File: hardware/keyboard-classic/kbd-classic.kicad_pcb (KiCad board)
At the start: 2 copper layers, 348 x 112.8 mm, 141 parts, among them J1 Controller, SW1 RT Arrow, SW10 Bracket_Open, SW11 6, SW12 Y, SW13 Return, SW14 Dash, SW15 5, SW16 T, SW17 Line Feed, SW18 Colon, SW19 4, SW2 LT Arrow, SW20 R, SW21 O, SW22 0, SW23 3, SW24 E, SW25 L, SW26 9, SW27 2, SW28 W, SW29 Period, SW3 Tilde, SW30 8, SW31 1, SW32 @ (OSI shift lock), SW33 Break, SW34 Rubout (OSI Break), SW35 R_Shift, SW36 P, SW37 Comma, SW38 K, SW39 L_Shift, SW4 I, SW40 Semicolon, SW41 M, SW42 J, SW43 Fwd_Slash, SW44 N, SW45 H, SW46 SPACE, SW47 B, SW48 G, SW49 TAB, SW5 Repeat, SW50 Z, SW51 V, SW52 F, SW53 CTRL, SW54 A, SW55 C, SW56 D, SW57 Backslash, SW58 Q, SW59 X, SW6 Bracket_Close, SW60 S, SW61 Power light, SW62 ESC, SW63 Spare, SW7 7, SW8 U, SW9 Caps_Lock

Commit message: Update the spacing comment to include spacing for keyboard cutout
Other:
- board text added: "Distances: Vertical: 0.75 inch Horizontal (1x - 1x): 0.75 inch Horizontal (1x - 1.5x): 0.9375 inch Horizontal (Row 1 left key -> Row 2 left key): 0.375 inch Horizontal (Row 2 left key -> Row 3 left key): 0.1875 inch Horizontal (Row 3 left key -> Row 4 left key): 0.1875 inch Horizontal (Row 4 left key -> Row 5 left key): -0.1875 inch Horizontal (Row 5 left key -> Space bar): 4.5 inch Center of key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"
- board text removed: "Distances: Vertical: 0.75 inch Horizontal (1x - 1x): 0.75 inch Horizontal (1x - 1.5x): 0.9375 inch Horizontal (Row 1 left key -> Row 2 left key): 0.375 inch Horizontal (Row 2 left key -> Row 3 left key): 0.1875 inch Horizontal (Row 3 left key -> Row 4 left key): 0.1875 inch Horizontal (Row 4 left key -> Row 5 left key): -0.1875 inch Horizontal (Row 5 left key -> Space bar): 4.5 inch"
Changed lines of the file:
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@@
   (gr_line (start 33.64738 180.34) (end 381.64738 180.34) (layer Edge.Cuts) (width 0.1))
   (gr_line (start 381.64738 67.564) (end 33.64738 67.564) (layer Edge.Cuts) (width 0.1))
-  (gr_text "Distances:\nVertical: 0.75 inch\nHorizontal (1x - 1x): 0.75 inch\nHorizontal (1x - 1.5x): 0.9375 inch\nHorizontal (Row 1 left key -> Row 2 left key): 0.375 inch\nHorizontal (Row 2 left key -> Row 3 left key): 0.1875 inch\nHorizontal (Row 3 left key -> Row 4 left key): 0.1875 inch\nHorizontal (Row 4 left key -> Row 5 left key): -0.1875 inch\nHorizontal (Row 5 left key -> Space bar): 4.5 inch" (at 38.4175 240.0681) (layer Cmts.User)
+  (gr_text "Distances:\nVertical: 0.75 inch\nHorizontal (1x - 1x): 0.75 inch\nHorizontal (1x - 1.5x): 0.9375 inch\nHorizontal (Row 1 left key -> Row 2 left key): 0.375 inch\nHorizontal (Row 2 left key -> Row 3 left key): 0.1875 inch\nHorizontal (Row 3 left key -> Row 4 left key): 0.1875 inch\nHorizontal (Row 4 left key -> Row 5 left key): -0.1875 inch\nHorizontal (Row 5 left key -> Space bar): 4.5 inch\nCenter of key to cutout edge: 0.36 inch" (at 38.4175 240.0681) (layer Cmts.User)
     (effects (font (size 2.54 2.54) (thickness 0.3048)) (justify left))
   )

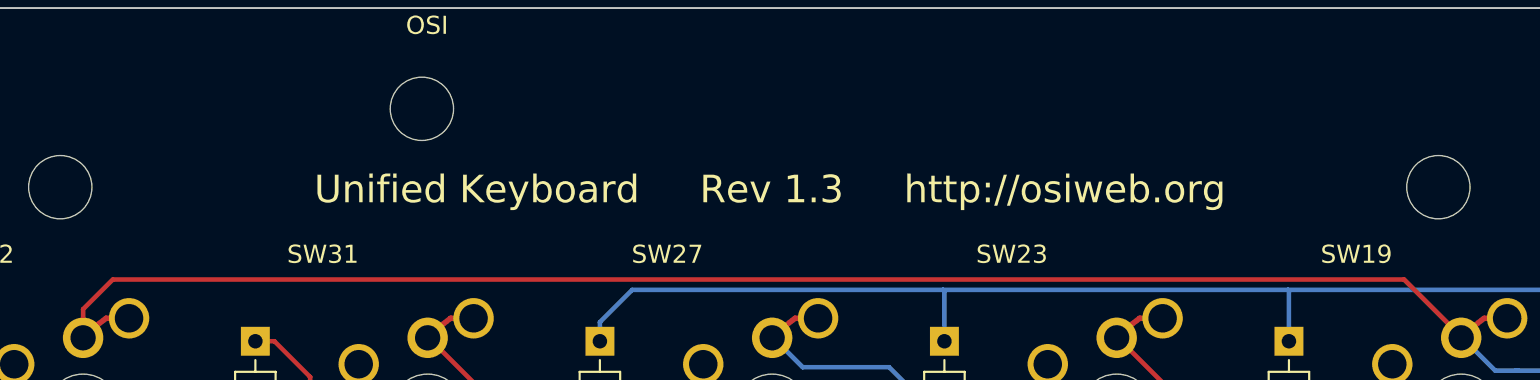
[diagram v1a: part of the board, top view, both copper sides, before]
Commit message: Update rev to 1.4
pcb: ajust cutout to account for 1.5u wide LEFT SHIFT
schematic: minor text format cleanup
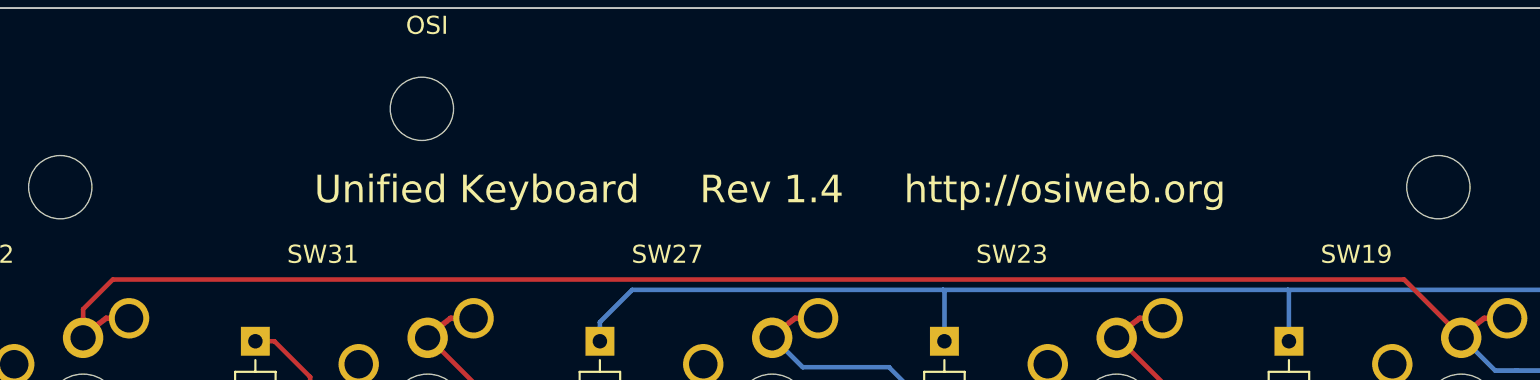
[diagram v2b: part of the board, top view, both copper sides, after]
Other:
- board text added: "Distances: Vertical: 0.75 inch Horizontal (1u - 1u): 0.75 inch Horizontal (1u - 1.5u): 0.9375 inch Horizontal (Row 1 left key -> Row 2 left key): 0.375 inch Horizontal (Row 2 left key -> Row 3 left key): 0.1875 inch Horizontal (Row 3 left key -> Row 4 left key): 0.1875 inch Horizontal (Row 4 left key -> Row 5 left key): -0.1875 inch Horizontal (Row 5 left key -> Space bar): 4.5 inch Center of key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"
- board text added: "Unified Keyboard Rev 1.4 http://osiweb.org"
- board text removed: "Distances: Vertical: 0.75 inch Horizontal (1x - 1x): 0.75 inch Horizontal (1x - 1.5x): 0.9375 inch Horizontal (Row 1 left key -> Row 2 left key): 0.375 inch Horizontal (Row 2 left key -> Row 3 left key): 0.1875 inch Horizontal (Row 3 left key -> Row 4 left key): 0.1875 inch Horizontal (Row 4 left key -> Row 5 left key): -0.1875 inch Horizontal (Row 5 left key -> Space bar): 4.5 inch Center of key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"
- board text removed: "Unified Keyboard Rev 1.3 http://osiweb.org"
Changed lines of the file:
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@@
   (general
     (thickness 1.6)
-    (drawings 44)
+    (drawings 40)
     (tracks 1105)
     (zones 0)
@@
     (title "Unified Retro Keyboard")
     (date 2019-08-25)
-    (rev 1.3)
+    (rev 1.4)
     (company OSIWeb.org)
     (comment 1 "Key matrix w/ LED")
@@
     (visible_elements 7FFFEFFF)
     (pcbplotparams
-      (layerselection 0x01000_7ffffffe)
+      (layerselection 0x11000_7ffffffe)
       (usegerberextensions false)
       (usegerberattributes false)
@@
   (gr_arc (start 376.64738 89.79916) (end 376.64738 91.57716) (angle -180) (layer Edge.Cuts) (width 0.1016))
   (gr_arc (start 376.64738 165.99916) (end 376.64738 167.77716) (angle -180) (layer Edge.Cuts) (width 0.1016))
-  (gr_line (start 73.71588 137.04316) (end 73.71588 117.99316) (layer B.Fab) (width 0.15))
-  (gr_line (start 73.71588 156.85516) (end 73.71588 175.14316) (layer B.Fab) (width 0.15))
-  (gr_line (start 78.47838 156.85516) (end 73.71588 156.85516) (layer B.Fab) (width 0.15))
-  (gr_line (start 78.47838 137.04316) (end 73.71588 137.04316) (layer B.Fab) (width 0.15))
-  (gr_line (start 78.47838 137.04316) (end 78.47838 156.85516) (layer B.Fab) (width 0.15))
+  (gr_line (start 73.71588 175.14316) (end 73.71588 117.99316) (layer B.Fab) (width 0.15))
   (gr_line (start 59.42838 98.94316) (end 68.95338 98.94316) (layer B.Fab) (width 0.15))
   (gr_line (start 43.17238 88.02116) (end 33.64738 88.02116) (layer Edge.Cuts) (width 0.1016))
@@
   (gr_line (start 33.64738 167.77716) (end 33.64738 180.34) (layer Edge.Cuts) (width 0.1016))
   (gr_arc (start 43.17238 89.79916) (end 43.17238 91.57716) (angle -180) (layer Edge.Cuts) (width 0.1016))
-  (gr_text "Unified Keyboard     Rev 1.3     http://osiweb.org" (at 106.553 77.597) (layer F.SilkS)
+  (gr_text "Unified Keyboard     Rev 1.4     http://osiweb.org" (at 106.553 77.597) (layer F.SilkS)
     (effects (font (size 1.524 1.524) (thickness 0.1778)))
   )
@@
   (gr_line (start 33.64738 180.34) (end 381.64738 180.34) (layer Edge.Cuts) (width 0.1))
   (gr_line (start 381.64738 67.564) (end 33.64738 67.564) (layer Edge.Cuts) (width 0.1))
-  (gr_text "Distances:\nVertical: 0.75 inch\nHorizontal (1x - 1x): 0.75 inch\nHorizontal (1x - 1.5x): 0.9375 inch\nHorizontal (Row 1 left key -> Row 2 left key): 0.375 inch\nHorizontal (Row 2 left key -> Row 3 left key): 0.1875 inch\nHorizontal (Row 3 left key -> Row 4 left key): 0.1875 inch\nHorizontal (Row 4 left key -> Row 5 left key): -0.1875 inch\nHorizontal (Row 5 left key -> Space bar): 4.5 inch\nCenter of key to cutout edge: 0.36 inch" (at 38.4175 240.0681) (layer Cmts.User)
+  (gr_text "Distances:\nVertical: 0.75 inch\nHorizontal (1u - 1u): 0.75 inch\nHorizontal (1u - 1.5u): 0.9375 inch\nHorizontal (Row 1 left key -> Row 2 left key): 0.375 inch\nHorizontal (Row 2 left key -> Row 3 left key): 0.1875 inch\nHorizontal (Row 3 left key -> Row 4 left key): 0.1875 inch\nHorizontal (Row 4 left key -> Row 5 left key): -0.1875 inch\nHorizontal (Row 5 left key -> Space bar): 4.5 inch\nCenter of key (1u) to vertical or side cutout edge: 0.36 inch\nCenter of key (1.5u) to side cutout edge: 0.5475 inch" (at 38.4175 240.0681) (layer Cmts.User)
     (effects (font (size 2.54 2.54) (thickness 0.3048)) (justify left))
   )

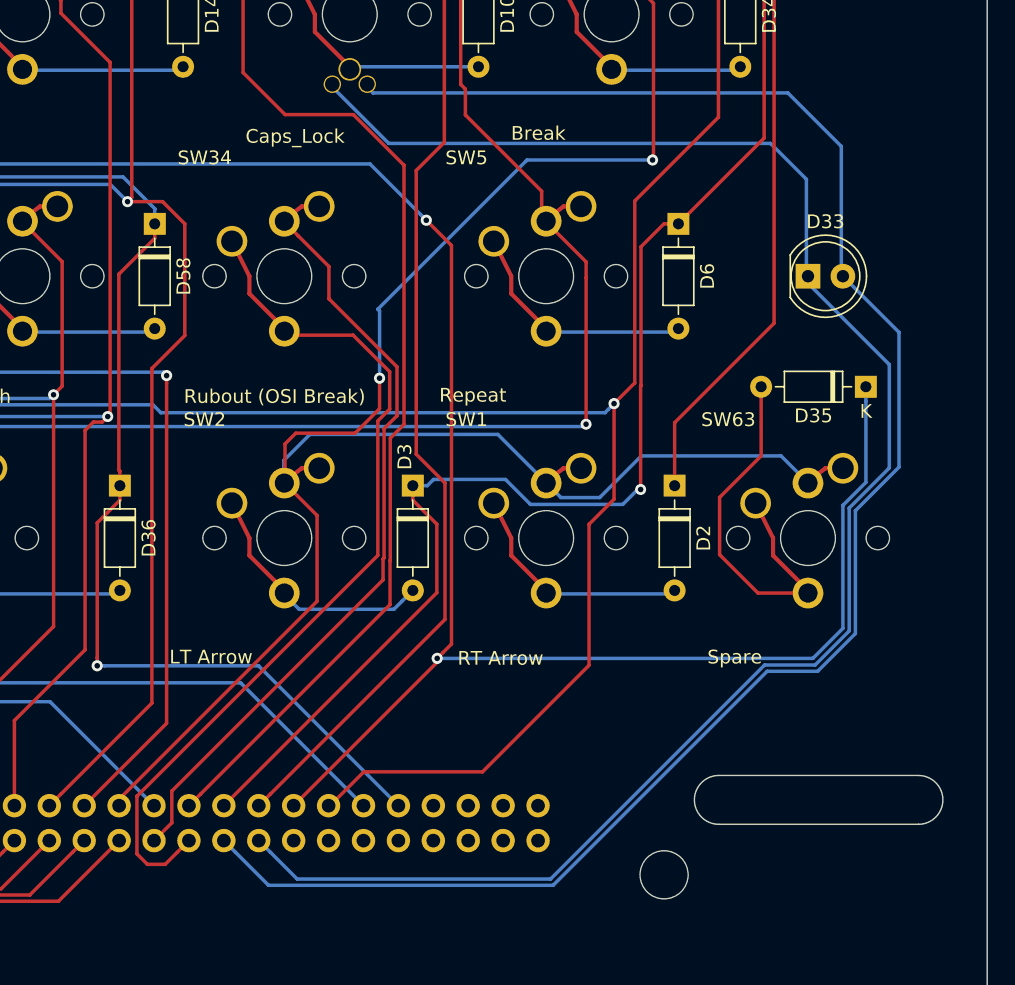
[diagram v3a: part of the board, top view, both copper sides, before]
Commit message: Moved spare LED from caps-lock to @ (OSI shift LOCK)
This allows the keymap to determine which LED is used, rather than requiring the
decision to be hardwired in at the time of assembly.  For the OSI keyboard, the
LED could be placed on the SHIFTLOCK key, at the far right LED, or in the
CAPSLOCK position, which is just to the left of the RETURN and not otherwise
populated in the OSI layout.
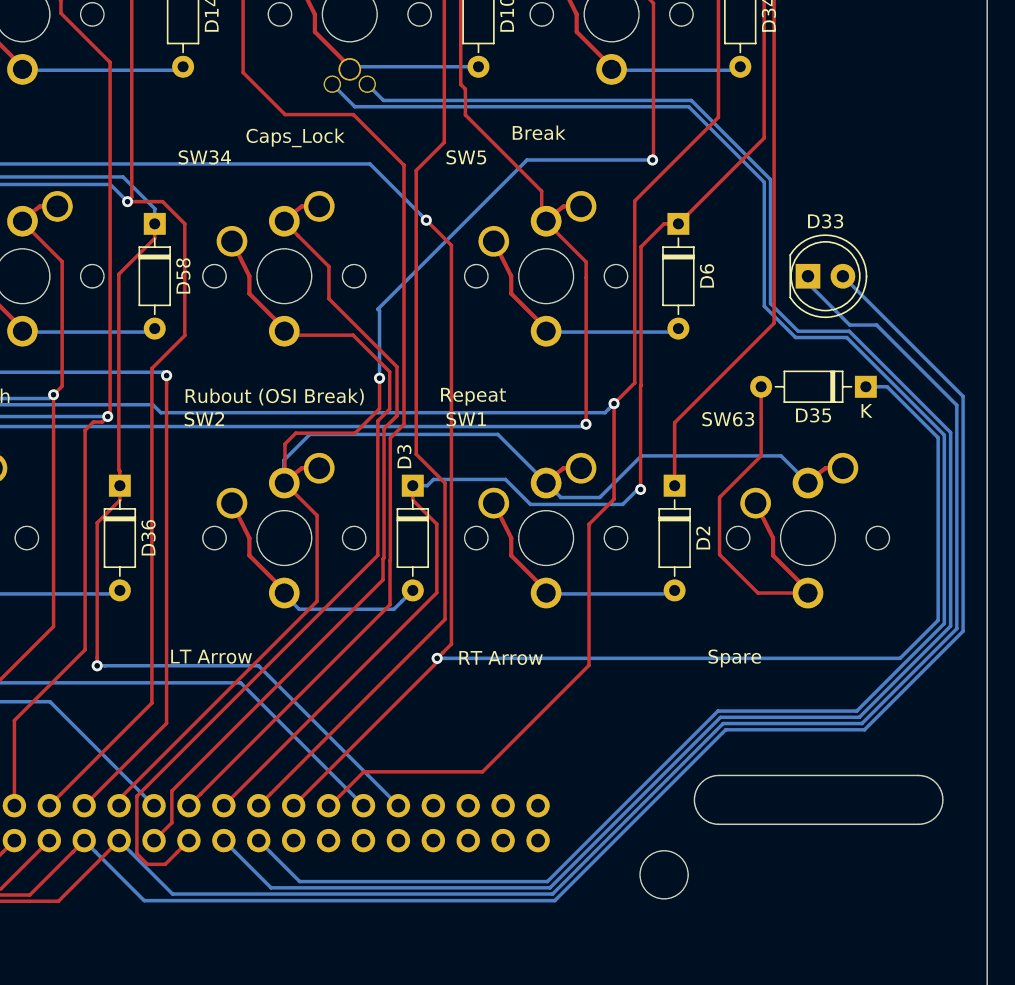
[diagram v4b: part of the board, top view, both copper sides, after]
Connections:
- J1 pad 14: Net-(J1-Pad14) -> Net-(D33-Pad2)
- J1 pad 16: Net-(J1-Pad16) -> Net-(D33-Pad1)
- J1 pad 22: Net-(D33-Pad2) -> Net-(J1-Pad22)
- J1 pad 24: Net-(D33-Pad1) -> Net-(J1-Pad24)
- SW32 pad 3: Net-(J1-Pad16) -> Net-(D33-Pad1)
- SW32 pad 4: Net-(J1-Pad14) -> Net-(D33-Pad2)
- SW9 pad 3: Net-(D33-Pad1) -> Net-(J1-Pad24)
- SW9 pad 4: Net-(D33-Pad2) -> Net-(J1-Pad22)
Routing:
- net Net-(J1-Pad22): track 0.00 -> 134.5 mm
- net Net-(J1-Pad24): track 0.00 -> 133.0 mm
- net Net-(J1-Pad16): track 68.5 -> 0.00 mm
- net Net-(J1-Pad14): track 61.5 -> 0.00 mm
- net Net-(D33-Pad1): track 125.7 -> 170.0 mm
- net Net-(D33-Pad2): track 129.9 -> 164.8 mm
- net /Row3: track 339.0 -> 348.0 mm

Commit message: Move LED current limit resistors to keyboard PCB
For better matching of current limit resistors to LEDs, the resistors are moved
to the keyboard matrix PCB, where they can be tuned for maximum brightness (at
100% duty cycle).  This allows consistent keyboard brightness when a single
interface PCB is swapped between keyboard matrices.
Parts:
- added R1: 470, Resistor_THT:R_Axial_DIN0207_L6.3mm_D2.5mm_P10.16mm_Horizontal, F.Cu at (69.8, 152.4)
- added R2: 470, Resistor_THT:R_Axial_DIN0207_L6.3mm_D2.5mm_P10.16mm_Horizontal, F.Cu at (310.4, 176.9)
- added R3: 470, Resistor_THT:R_Axial_DIN0207_L6.3mm_D2.5mm_P10.16mm_Horizontal, F.Cu at (370.8, 116.8)
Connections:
- J1 pad 14: Net-(D33-Pad2) -> Net-(J1-Pad14)
- SW61 pad 3: Net-(J1-Pad8) -> Net-(R1-Pad1)
- SW9 pad 4: Net-(J1-Pad22) -> Net-(R3-Pad2)
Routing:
- net Net-(R3-Pad2): track 0.00 -> 40.2 mm
- net Net-(J1-Pad22): track 134.5 -> 108.3 mm
- net Net-(R1-Pad1): track 0.00 -> 24.5 mm
- net Net-(J1-Pad8): track 246.6 -> 261.8 mm
- net Net-(J1-Pad14): track 0.00 -> 10.7 mm
- net Net-(D33-Pad2): track 164.8 -> 174.0 mm, vias 0 -> 1
- net Net-(J1-Pad10): track 62.3 -> 63.6 mm
- net Net-(J1-Pad12): track 60.8 -> 61.6 mm
- net Net-(D33-Pad1): track 170.0 -> 169.5 mm

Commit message: Multiple fixes to classic keyboard for fit and build ease
- remove material from PCB to allow keyboard to fit in Apple II case

- enlarge center hole on cherry MX footprints slightly, to 0.160" to allow
slightly more tolerance, which eases assembly.

- include holes for LEDs on futaba aligner

- include extra pads on main PCB for LEDs with futaba keys

- Add LED on LINE FEED which maps to REPEAT/CAPSLOCK on Apple II keymap
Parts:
- removed the REF** at (263.8, 174.3)
- removed the REF** at (263.8, 159.0)
- removed Stabilizer (x2): MountingHole_3.5mm, MountingHole:MountingHole_3.5mm
- added D62: LED, LED_THT:LED_D2.0mm_W4.8mm_H2.5mm_FlatTop, F.Cu at (84.1, 175.5)
- added D63: LED, LED_THT:LED_D2.0mm_W4.8mm_H2.5mm_FlatTop, F.Cu at (334.1, 118.4)
- added D64: LED, LED_THT:LED_D2.0mm_W4.8mm_H2.5mm_FlatTop, F.Cu at (293.7, 137.4)
- added D65: LED, LED_THT:LED_D2.0mm_W4.8mm_H2.5mm_FlatTop, F.Cu at (286.5, 118.4)
- SW17: value Line Feed -> Line_Feed; footprint unikbd:Key_MX -> unikbd:Key_MX_LED
- SW32: value @ (OSI shift lock) -> @ (OSI ShiftLock)
- SW46: footprint unikbd:Key_MX -> unikbd:Key_MX_Spacebar_5.25
- SW61: value Power light -> Power Light
- moved D33 3.81 mm to (364.8, 127.9)
- moved R3 2.79 mm to (368.0, 116.8)
- moved D4 2.54 mm to (368.0, 95.0)
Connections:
- J1 pad 24: Net-(J1-Pad24) -> Net-(D63-Pad1)
- J1 pad 8: Net-(J1-Pad8) -> Net-(D62-Pad1)
- R1 pad 2: Net-(J1-Pad8) -> Net-(J1-Pad6)
- R3 pad 2: Net-(R3-Pad2) -> Net-(D63-Pad2)
- SW17 pad 3: (no net) -> Net-(D63-Pad1)
- SW17 pad 4: (no net) -> Net-(D63-Pad2)
- SW32 pad 3: Net-(D33-Pad1) -> Net-(D33-Pad2)
- SW32 pad 4: Net-(D33-Pad2) -> Net-(D33-Pad1)
- SW61 pad 4: Net-(J1-Pad6) -> Net-(D62-Pad1)
- SW9 pad 3: Net-(J1-Pad24) -> Net-(D63-Pad1)
- SW9 pad 4: Net-(R3-Pad2) -> Net-(D63-Pad2)
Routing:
- net Net-(J1-Pad8): track 261.8 -> 0.00 mm
- net Net-(D62-Pad1): track 0.00 -> 248.0 mm, vias 0 -> 1
- net Net-(D63-Pad1): track 0.00 -> 196.7 mm
- net Net-(J1-Pad24): track 132.9 -> 0.00 mm
- net Net-(D63-Pad2): track 0.00 -> 110.9 mm
- net Net-(R3-Pad2): track 40.2 -> 0.00 mm
- net Net-(J1-Pad6): track 240.2 -> 259.7 mm
- net Net-(D33-Pad2): track 174.0 -> 188.8 mm, vias 1 -> 2
- net /Row6: track 276.0 -> 284.2 mm
- net Net-(J1-Pad22): track 108.3 -> 114.4 mm
- net Net-(D4-Pad2): track 22.5 -> 17.3 mm
- net Net-(D62-Pad2): track 24.5 -> 29.1 mm
- net /Row5: track 275.8 -> 271.8 mm, vias 2 -> 3
- net Net-(D33-Pad1): track 169.5 -> 171.8 mm
- net /Col7: track 385.5 -> 387.3 mm
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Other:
- outline, holes or cut-outs redrawn

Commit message: Fixes for classic keyboard outline and mounting hole patters
- Adjust upper right corner circular cutout for AppleII+ case fit.

- Adjust OSI mounting hole pattern for improved fit.

- Changed OSI mount holes along top of keyboard to slots, to fit both C2P (542
keyboard) and C4P (542 Rev B/c keyboards).

- PCB and aligners must be slightly taller to accommodate the slots along the
top row
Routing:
- net Net-(D63-Pad1): track 196.7 -> 195.0 mm
- net /Row3: track 349.3 -> 348.6 mm
- net Net-(D33-Pad2): track 188.8 -> 188.2 mm
- net Net-(J1-Pad22): track 114.4 -> 113.9 mm
- net Net-(D33-Pad1): track 171.8 -> 171.2 mm
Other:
- board size 348 x 112.8 mm -> 346.1 x 116.8 mm
- board text added: "Unified Keyboard Rev 1.7 http://osiweb.org"
- board text removed: "Unified Keyboard Rev 1.4 http://osiweb.org"
